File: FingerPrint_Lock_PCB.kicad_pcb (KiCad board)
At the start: 2 copper layers, 55.9 x 49.5 mm, 16 parts, among them J1 Arduino_Digital1, J2 Arduino_Digital2, J3 Arduino_Analog, J4 Arduino_Power, J5 Sensor, J6 Relay, J7 LCD, SW1 SW_Push_Dual, SW2 SW_Push_Dual, SW3 SW_Push_Dual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

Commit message: Post-design-review revisions
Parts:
- SW1, SW2, SW3, SW4: value SW_Push_Dual -> SW_Push
- moved SW3 0.05 mm to (158.8, 102.1)
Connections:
- net /GND renamed GND
- net /VIN renamed +12V
- J1 pad 7: /D1 -> unconnected-(J1-Pad7)
- J1 pad 8: /D0 -> unconnected-(J1-Pad8)
- J2 pad 1: /UL2 -> unconnected-(J2-Pad1)
- J2 pad 2: /UL1 -> unconnected-(J2-Pad2)
- J2 pad 3: /AREF -> unconnected-(J2-Pad3)
- J2 pad 5: /D13 -> unconnected-(J2-Pad5)
- J2 pad 6: /D12 -> unconnected-(J2-Pad6)
- J2 pad 7: /D11 -> unconnected-(J2-Pad7)
- J2 pad 8: /D10 -> unconnected-(J2-Pad8)
- J2 pad 9: /D9 -> unconnected-(J2-Pad9)
- J3 pad 1: /A0 -> unconnected-(J3-Pad1)
- J3 pad 2: /A1 -> unconnected-(J3-Pad2)
- J3 pad 3: /A2 -> unconnected-(J3-Pad3)
- J3 pad 4: /A3 -> unconnected-(J3-Pad4)
- J4 pad 1: /UL3 -> unconnected-(J4-Pad1)
- J4 pad 2: /IOREF -> unconnected-(J4-Pad2)
- J4 pad 3: /RESET -> unconnected-(J4-Pad3)
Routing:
- net GND: vias 0 -> 20
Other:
- board text added: "A5 A4 A3 A2 A1 A0"
- board text added: "D0 D1 D2 D3 D4 D5 D6 D7"
- board text added: "D8 D9 D10 D11 D12 D13 GND REF"
- board text added: "Vin GND GND 5V 3V3 RST REF"

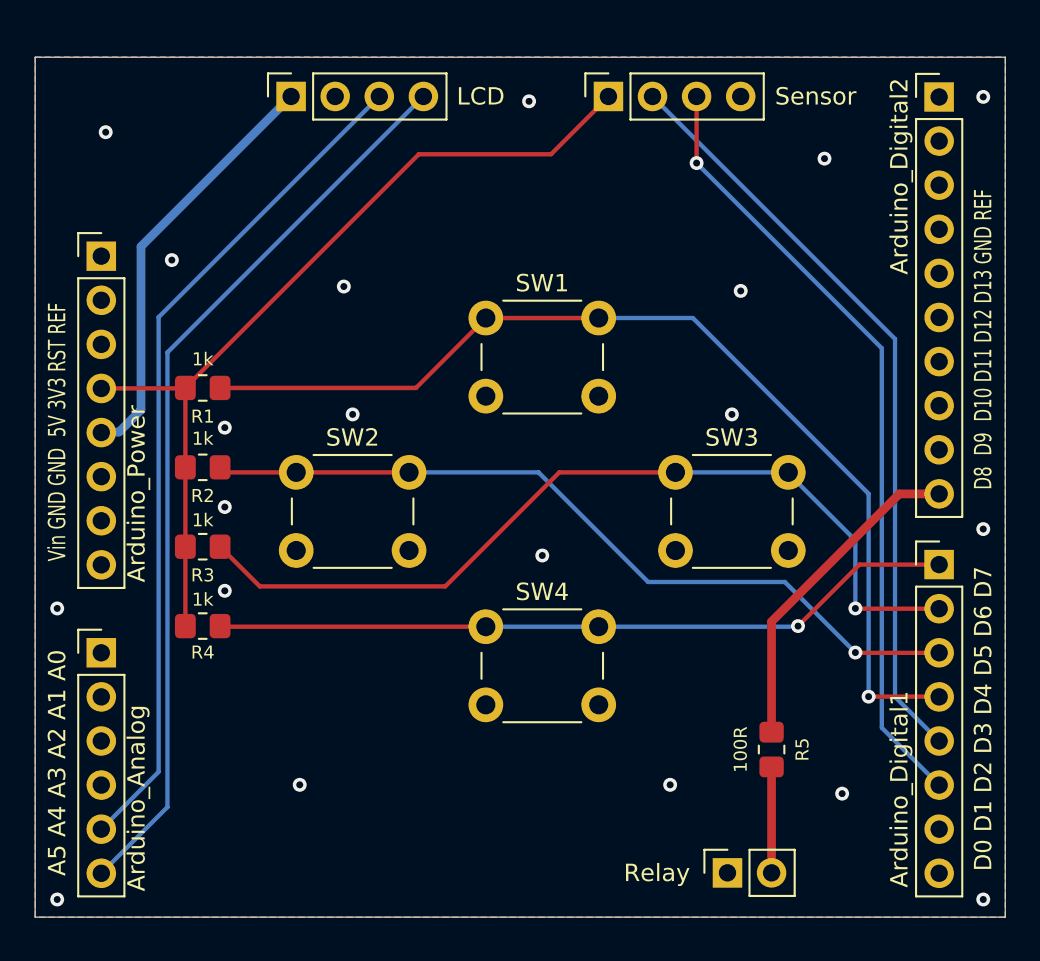
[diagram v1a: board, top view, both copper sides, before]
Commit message: Minor changes; updated silkscreen
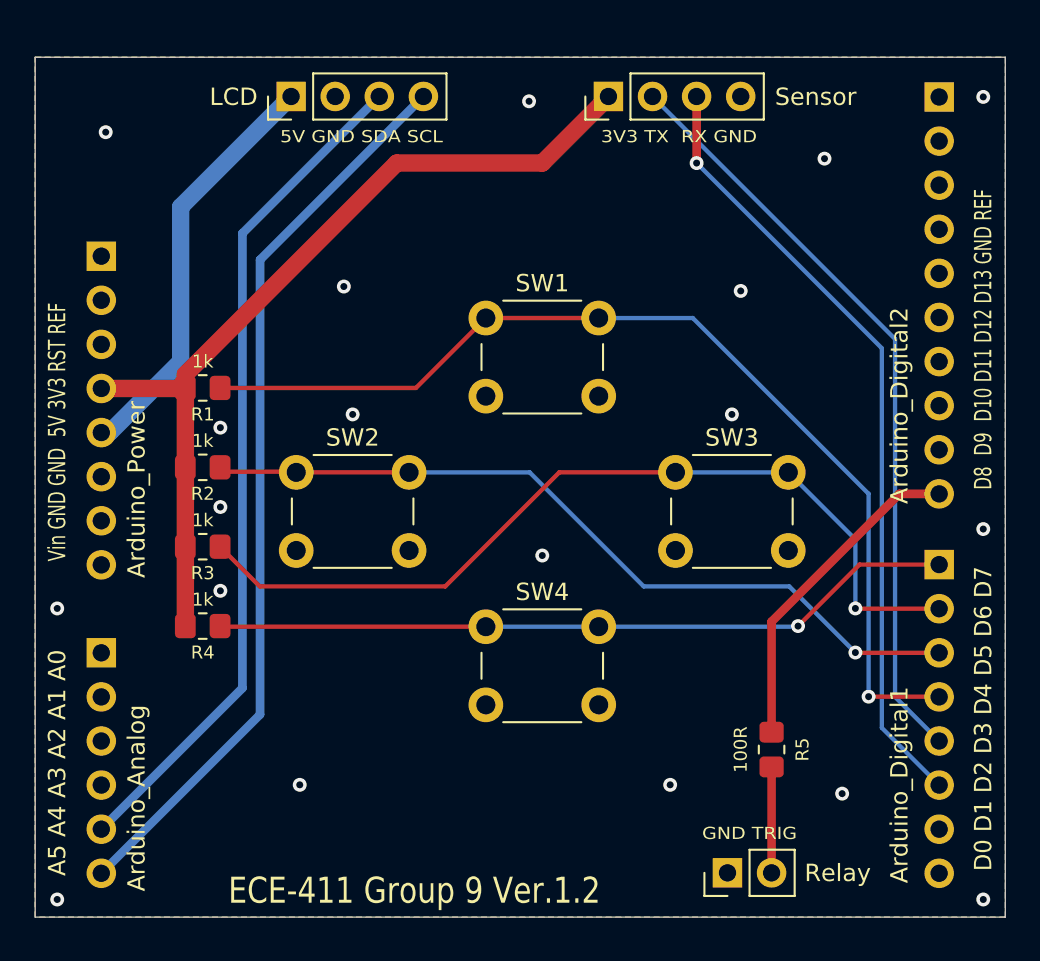
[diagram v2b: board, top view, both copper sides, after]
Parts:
- J1, J2, J3, J4: moved to B.Cu
- J5, J7: footprint Connector_PinSocket_2.54mm:PinSocket_1x04_P2.54mm_Vertical -> Connector_PinHeader_2.54mm:PinHeader_1x04_P2.54mm_Vertical
- J6: footprint Connector_PinSocket_2.54mm:PinSocket_1x02_P2.54mm_Vertical -> Connector_PinHeader_2.54mm:PinHeader_1x02_P2.54mm_Vertical
- SW1, SW2, SW3, SW4: value SW_Push -> 6x5mm; footprint Button_Switch_THT:SW_PUSH_6mm_H9.5mm -> Button_Switch_THT:SW_PUSH_6mm_H5mm
- turned J1 to 180 degrees
- turned J2 to 180 degrees
- turned J3 to 180 degrees
- turned J4 to 180 degrees
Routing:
- net GND: vias 20 -> 19
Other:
- board text added: "3V3 TX RX GND"
- board text added: "5V GND SDA SCL"
- board text added: "ECE-411 Group 9 Ver.1.2"
- board text added: "GND TRIG"
